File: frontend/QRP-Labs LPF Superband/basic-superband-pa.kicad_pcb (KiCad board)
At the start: 2 copper layers, 64.5 x 60 mm, 82 parts, among them CN1 EDGE, K1 D3002, K2 D3002, P1 BNC, P2 VFWD, P3 Ext PTT, P4 12-13.8v, Q1 FDV301, Q2 FDV301, Q3 RD16HHF1, T2 8:1, T3 4:1, T4 OUT_TRANSF, U1 LP2951-50D

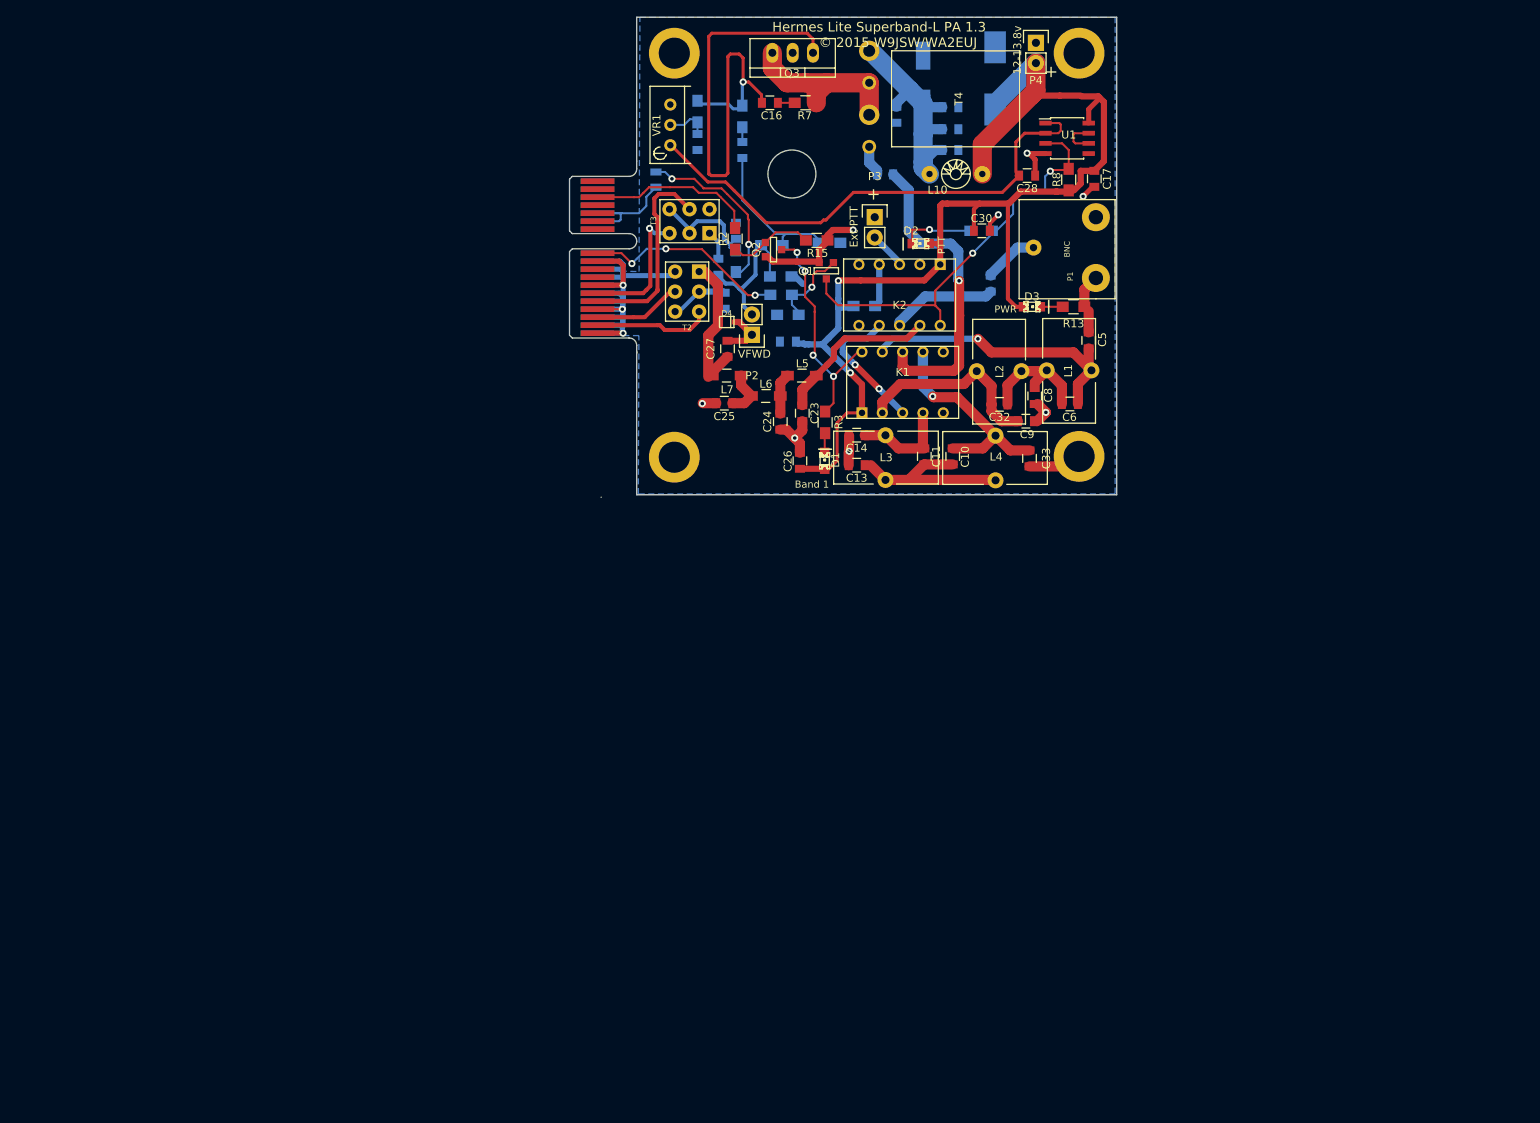
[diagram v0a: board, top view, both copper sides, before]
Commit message: Further updates to the pre-V2 amp
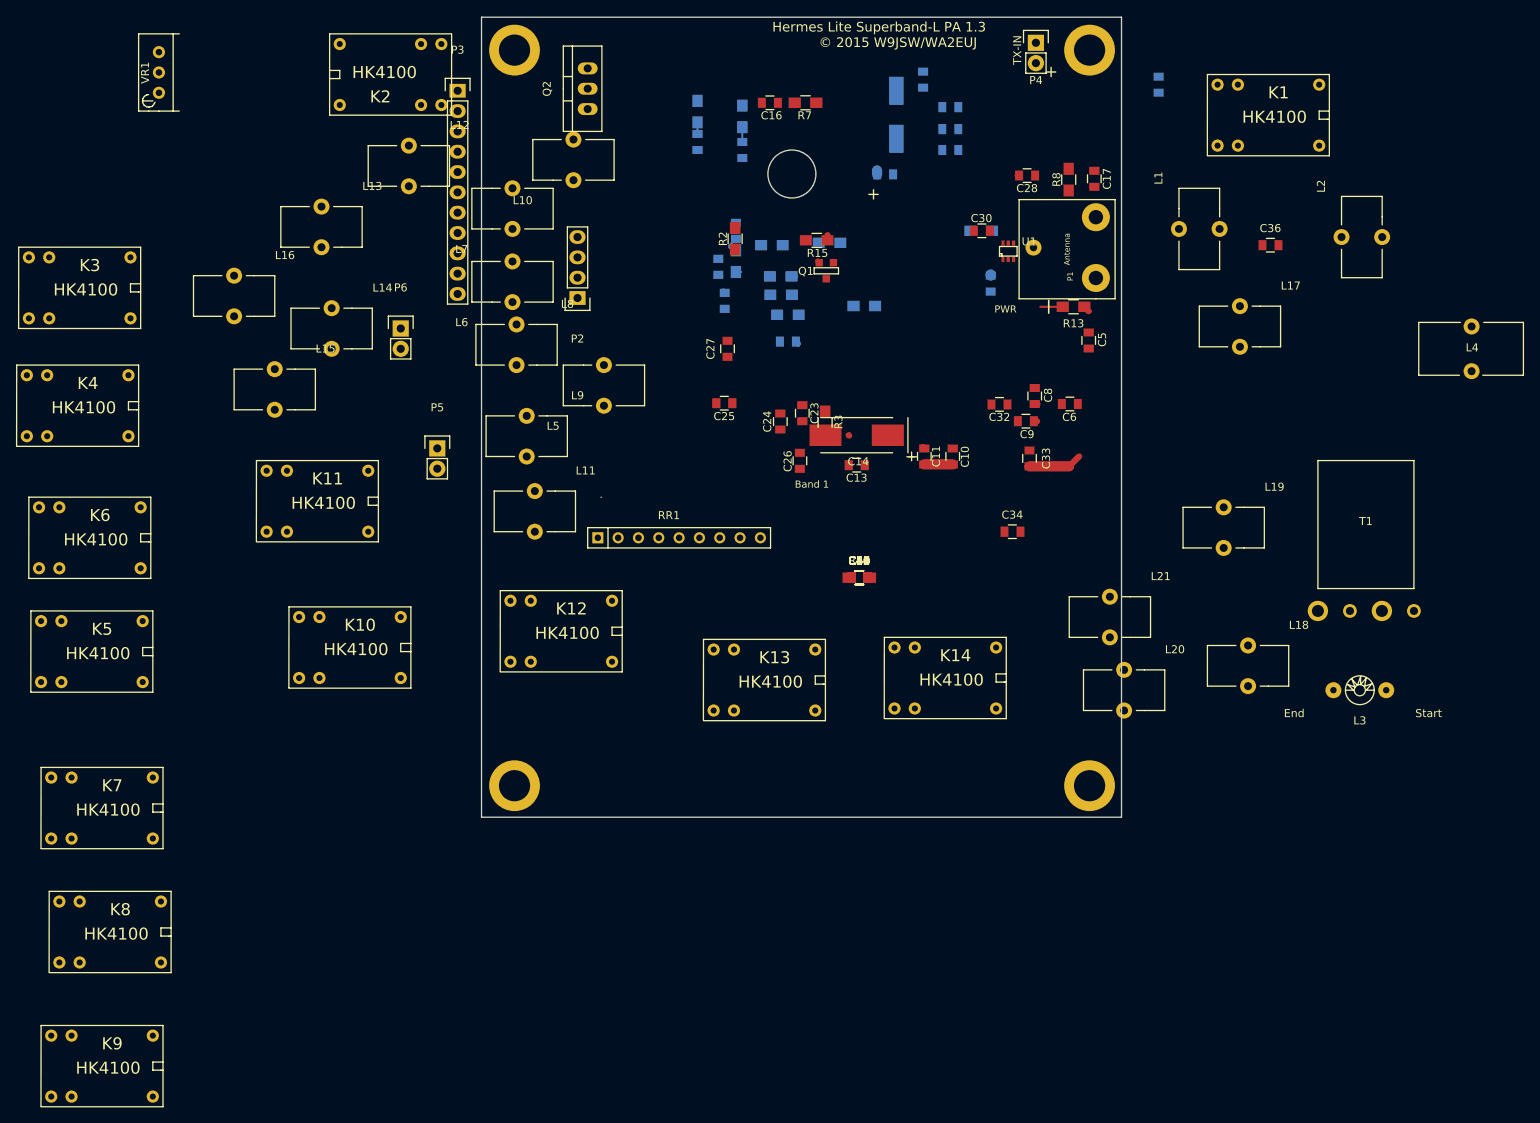
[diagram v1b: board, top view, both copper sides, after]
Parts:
- removed CN1: EDGE, HERMESLITE:EDGE
- removed D1: YEL LED (Band1), LEDs:LED-0805
- removed D2: RED LED (PTT), LEDs:LED-0805
- removed D3: GRN LED (PWR ON), LEDs:LED-0805
- removed D4: DIODESCH2, HERMESLITE:SOD323
- removed FB1: FB, SMD_Packages:SMD-0805
- removed Q3: RD16HHF1, Transistors_TO-220:TO-220_Neutral123_Vertical
- removed T2: 8:1, HERMESLITE:TRANSF
- removed T3: 4:1, HERMESLITE:TRANSF
- removed T4: OUT_TRANSF, HERMESLITE:OUT_TRANSF
- added C34: C, HERMESLITE:C_0805, F.Cu at (181.4, 99.3)
- added C35, C37, C38, C45, C46, C47, C48, C49, C50, C57, C58, C59, C60, C61, C62: C, HERMESLITE:C_0805, F.Cu at (162.2, 105.1)
- added C36: C, HERMESLITE:C_0805, F.Cu at (213.6, 63.5)
- added C39, C40, C41, C42, C43, C44, C51, C52, C53, C54, C55, C56: DNI, HERMESLITE:C_0805, F.Cu at (162.2, 105.1)
- added K10: HK4100, HERMESLITE:HK4100, F.Cu at (98.6, 113.8)
- added K11: HK4100, HERMESLITE:HK4100, F.Cu at (94.5, 95.5)
- added K12: HK4100, HERMESLITE:HK4100, F.Cu at (125.0, 111.8)
- added K13: HK4100, HERMESLITE:HK4100, F.Cu at (150.4, 117.9)
- added K14: HK4100, HERMESLITE:HK4100, F.Cu at (173.0, 117.6)
- added K3: HK4100, HERMESLITE:HK4100, F.Cu at (64.8, 68.8)
- added K4: HK4100, HERMESLITE:HK4100, F.Cu at (64.5, 83.6)
- added K5: HK4100, HERMESLITE:HK4100, F.Cu at (66.3, 114.3)
- added K6: HK4100, HERMESLITE:HK4100, F.Cu at (66.0, 100.1)
- added K7: HK4100, HERMESLITE:HK4100, F.Cu at (67.6, 133.9)
- added K8: HK4100, HERMESLITE:HK4100, F.Cu at (68.6, 149.4)
- added K9: HK4100, HERMESLITE:HK4100, F.Cu at (67.6, 166.1)
- added L11: INDUCTOR, Choke_Toroid_ThroughHole:Choke_Toroid_5x10mm_Vertical, F.Cu at (116.6, 99.3)
- added L12: INDUCTOR, Choke_Toroid_ThroughHole:Choke_Toroid_5x10mm_Vertical, F.Cu at (100.8, 56.1)
- added L13: INDUCTOR, Choke_Toroid_ThroughHole:Choke_Toroid_5x10mm_Vertical, F.Cu at (89.9, 63.8)
- added L14: INDUCTOR, Choke_Toroid_ThroughHole:Choke_Toroid_5x10mm_Vertical, F.Cu at (91.2, 76.5)
- added L15: INDUCTOR, Choke_Toroid_ThroughHole:Choke_Toroid_5x10mm_Vertical, F.Cu at (84.1, 84.1)
- added L16: INDUCTOR, Choke_Toroid_ThroughHole:Choke_Toroid_5x10mm_Vertical, F.Cu at (79.0, 72.4)
- added L17: INDUCTOR, Choke_Toroid_ThroughHole:Choke_Toroid_5x10mm_Vertical, F.Cu at (204.7, 76.2)
- added L18: INDUCTOR, Choke_Toroid_ThroughHole:Choke_Toroid_5x10mm_Vertical, F.Cu at (205.7, 118.6)
- added L19: INDUCTOR, Choke_Toroid_ThroughHole:Choke_Toroid_5x10mm_Vertical, F.Cu at (202.7, 101.3)
- added L20: INDUCTOR, Choke_Toroid_ThroughHole:Choke_Toroid_5x10mm_Vertical, F.Cu at (190.2, 121.7)
- added L21: INDUCTOR, Choke_Toroid_ThroughHole:Choke_Toroid_5x10mm_Vertical, F.Cu at (188.5, 112.5)
- added L8: INDUCTOR, Choke_Toroid_ThroughHole:Choke_Toroid_5x10mm_Vertical, F.Cu at (114.3, 78.5)
- added L9: INDUCTOR, Choke_Toroid_ThroughHole:Choke_Toroid_5x10mm_Vertical, F.Cu at (115.6, 89.9)
- added P5: RX IN, Pin_Headers:Pin_Header_Straight_1x02, F.Cu at (109.5, 88.9)
- added P6: 12-13.8v, Pin_Headers:Pin_Header_Straight_1x02, F.Cu at (104.9, 73.9)
- added R17: 270, Resistors_SMD:R_0805_HandSoldering, F.Cu at (162.2, 105.1)
- added RR1: 10K, Discret:r_pack8, F.Cu at (139.7, 100.1)
- added T1: OUT_TRANSF, HERMESLITE:OUT_TRANSF, F.Cu at (225.6, 109.2)
- C10: value C -> 1uF
- C11, C13, C8, C9: value C -> 0.1uF
- C14: value C -> 47uF 25V; footprint HERMESLITE:C_0805 -> Capacitors_Tantalum_SMD:TantalC_SizeD_EIA-7343_HandSoldering
- C17: value 1uF -> 0.1uF
- C19: value 0.1uF -> 4700pF
- C2: value 0.1 uF -> 78pf
- C20: value 0.1uF -> 10uF 25V; footprint HERMESLITE:C_0805 -> Capacitors_Tantalum_SMD:TantalC_SizeC_EIA-6032_HandSoldering
- C21: value 4700pF -> C
- C22: value 10uF 25V -> C; footprint Capacitors_Tantalum_SMD:TantalC_SizeC_EIA-6032_HandSoldering -> HERMESLITE:C_0805
- C23: value 56pf -> C
- C24, C25: value 156pf -> C
- C26: value 0.1uF -> C
- C27: value 56pf -> DNI
- C28: value 1uF -> DNI
- C29, C30, C31: value 0.1uF -> DNI
- C3: value 0.1 uF -> 12pf
- C32: value C -> DNI
- C4: value 0.1uF -> 150pf
- C5: value C -> 30pf
- C6: value C -> 56pf
- C7: value 47uF 25V -> 1uF; footprint Capacitors_Tantalum_SMD:TantalC_SizeD_EIA-7343_HandSoldering -> HERMESLITE:C_0805
- K1, K2: value D3002 -> HK4100; footprint HERMESLITE:D3002 -> HERMESLITE:HK4100
- L1: value INDUCTOR -> 302.5nH; footprint Choke_Toroid_ThroughHole:Choke_Toroid_6,5x13mm_Vertical -> Choke_Toroid_ThroughHole:Choke_Toroid_5x10mm_Vertical
- L10: value FT37-43 11T #26 -> INDUCTOR; footprint Choke_Toroid_ThroughHole:Choke_Toroid_horizontal_Diameter3-5mm_Amidon-T12 -> Choke_Toroid_ThroughHole:Choke_Toroid_5x10mm_Vertical
- L2: value INDUCTOR -> 250nH; footprint Choke_Toroid_ThroughHole:Choke_Toroid_6,5x13mm_Vertical -> Choke_Toroid_ThroughHole:Choke_Toroid_5x10mm_Vertical
- L3: value INDUCTOR -> FT37-43 11T #26; footprint Choke_Toroid_ThroughHole:Choke_Toroid_6,5x13mm_Vertical -> Choke_Toroid_ThroughHole:Choke_Toroid_horizontal_Diameter3-5mm_Amidon-T12
- L5, L6, L7: footprint Choke_SMD:Choke_SMD_1206_Standard -> Choke_Toroid_ThroughHole:Choke_Toroid_5x10mm_Vertical
- P1: value BNC -> Antenna
- P2: value VFWD -> CONN_01X04; footprint Pin_Headers:Pin_Header_Straight_1x02 -> Pin_Headers:Pin_Header_Straight_1x04
- P3: value Ext PTT -> PA Control; footprint Pin_Headers:Pin_Header_Straight_1x02 -> Pin_Headers:Pin_Header_Straight_1x11
- P4: value 12-13.8v -> TX-IN
- Q2: value FDV301 -> RD16HHF1; footprint HERMESLITE:SOT-23-GDS -> Transistors_TO-220:TO-220_Neutral123_Vertical
- R1: value 499 -> 2.7k
- R10: value 270 -> 18
- R11: value 18 -> 61
- R13, R9: value 4.99k -> 247
- R14: value 4.99k -> 10k
- R15: value 10k -> 6.8
- R2: value 499 -> 120
- R3: value 4.99k -> 51
- R4: value 0 -> 120
- R5: value 6.8 -> 247
- R6: value 10k -> 61
- R7: value 270 -> 247
- R8: value 10k -> 270
- U1: value LP2951-50D -> PE4259-53; footprint Housings_SOIC:SOIC-8_3.9x4.9mm_Pitch1.27mm -> HERMESLITE:sc70-6
- moved K2 69.3 mm to (103.6, 42.2)
- moved VR1 64.3 mm to (74.7, 44.5)
- moved L3 61.8 mm to (224.8, 119.1)
- moved L4 61.1 mm to (232.2, 79.8)
- moved K1 56.6 mm to (213.4, 47.2)
- moved P3 54.5 mm to (112.0, 44.2)
- moved L2 48.2 mm to (227.6, 67.6)
- moved MH 45.7 mm to (119.1, 131.1)
- moved L10 42.9 mm to (131.6, 50.3)
- moved MH 41.2 mm to (191.0, 131.1)
- moved L7 31.9 mm to (124.0, 56.4)
- moved L6 31.5 mm to (124.0, 65.5)
- moved Q2 30.7 mm to (128.3, 43.9)
- moved L1 24.7 mm to (207.3, 66.5)
- moved P2 22.3 mm to (127.0, 70.1)
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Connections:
- C1 pad 1: GND -> Net-(C1-Pad1)
- C10 pad 1: Net-(C10-Pad1) -> GND
- C11 pad 2: Net-(C10-Pad1) -> Net-(C11-Pad2)
- C12 pad 1: GND -> Net-(C12-Pad1)
- C12 pad 2: Net-(C12-Pad2) -> GND
- C13 pad 1: Net-(C10-Pad1) -> Net-(C12-Pad1)
- C14 pad 1: Net-(C11-Pad1) -> Net-(C12-Pad1)
- C15 pad 2: Net-(C15-Pad2) -> TX-OUT
- C16 pad 1: Net-(C16-Pad1) -> GND
- C17 pad 1: Net-(C17-Pad1) -> GND
- C17 pad 2: GND -> Net-(C16-Pad2)
- C18 pad 1: Net-(C18-Pad1) -> GND
- C18 pad 2: Net-(C18-Pad2) -> Net-(C16-Pad2)
- C19 pad 2: Net-(C1-Pad2) -> Net-(C16-Pad2)
- C2 pad 1: Net-(C2-Pad1) -> Net-(C1-Pad2)
- C20 pad 1: GND -> Net-(C16-Pad2)
- C20 pad 2: Net-(C1-Pad2) -> GND
- C21 pad 1: GND -> Net-(C21-Pad1)
- C21 pad 2: Net-(C1-Pad2) -> GND
- C22 pad 1: Net-(C1-Pad2) -> Net-(C22-Pad1)
- C26 pad 1: GND -> Net-(C26-Pad1)
- C26 pad 2: Net-(C17-Pad1) -> GND
- C27 pad 2: GND -> Net-(C21-Pad1)
- C28 pad 1: GND -> Net-(C28-Pad1)
- C28 pad 2: Net-(C28-Pad2) -> Net-(C22-Pad1)
- C29 pad 2: Net-(C29-Pad2) -> Net-(C23-Pad1)
- C3 pad 2: GND -> Net-(C1-Pad2)
- C30 pad 1: Net-(C17-Pad1) -> Net-(C30-Pad1)
- C30 pad 2: GND -> Net-(C24-Pad1)
- C31 pad 1: Net-(C17-Pad1) -> Net-(C31-Pad1)
- C31 pad 2: GND -> Net-(C25-Pad1)
- C32 pad 2: Net-(C32-Pad2) -> Net-(C26-Pad1)
- C33 pad 1: Net-(C10-Pad2) -> Net-(C27-Pad1)
- C4 pad 1: Net-(C4-Pad1) -> Net-(C3-Pad1)
- C4 pad 2: Net-(C4-Pad2) -> GND
- C5 pad 2: GND -> Net-(C3-Pad1)
- C6 pad 2: Net-(C32-Pad1) -> GND
- C7 pad 1: Net-(C17-Pad1) -> GND
- C7 pad 2: GND -> +5V
- C8 pad 1: Net-(C32-Pad1) -> Net-(C8-Pad1)
- C8 pad 2: GND -> Net-(C8-Pad2)
- C9 pad 1: Net-(C32-Pad2) -> GND
- C9 pad 2: GND -> Net-(C9-Pad2)
- K1 pad 1: Net-(C17-Pad1) -> Net-(K1-Pad1)
- K1 pad 2: Net-(C32-Pad2) -> /PTT
- K1 pad 3: Net-(K1-Pad3) -> Net-(C5-Pad1)
- K1 pad 4: Net-(C11-Pad1) -> Net-(K1-Pad4)
- K1 pad 5: (no net) -> +5V
- K1 pad 6: (no net) -> TX-IN
- K2 pad 1: Net-(C17-Pad1) -> GND
- K2 pad 2: GND -> /Band0
- K2 pad 4: Net-(K2-Pad4) -> Net-(C21-Pad1)
- K2 pad 5: (no net) -> +5V
- K2 pad 6: (no net) -> TX-OUT
- L1 pad 1: Net-(C5-Pad1) -> Net-(C1-Pad2)
- L1 pad 2: Net-(C32-Pad1) -> Net-(C3-Pad1)
- L10 pad 1: Net-(C17-Pad1) -> Net-(C27-Pad1)
- L10 pad 2: Net-(C1-Pad2) -> Net-(C39-Pad1)
- L2 pad 1: Net-(C32-Pad1) -> Net-(C3-Pad1)
- L2 pad 2: Net-(C32-Pad2) -> Net-(C5-Pad1)
- L3 pad 1: Net-(C11-Pad1) -> Net-(C12-Pad1)
- L3 pad 2: Net-(C10-Pad1) -> Net-(C16-Pad2)
- L4 pad 1: Net-(C10-Pad1) -> Net-(C21-Pad1)
- L4 pad 2: Net-(C10-Pad2) -> Net-(C27-Pad1)
- L5 pad 1: Net-(C23-Pad1) -> Net-(C22-Pad1)
- L5 pad 2: Net-(C24-Pad1) -> Net-(C28-Pad1)
- L6 pad 1: Net-(C24-Pad1) -> Net-(C23-Pad1)
- L6 pad 2: Net-(C25-Pad1) -> Net-(C29-Pad1)
- L7 pad 1: Net-(C25-Pad1) -> Net-(C24-Pad1)
- L7 pad 2: Net-(C27-Pad1) -> Net-(C30-Pad1)
- P1 pad 1: Net-(C18-Pad1) -> Net-(C1-Pad1)
- P2 pad 2: Net-(C4-Pad1) -> +3.3V
- P3 pad 1: GND -> /Band0
- P3 pad 2: Net-(K2-Pad3) -> /Band1
- P4 pad 2: Net-(C17-Pad1) -> Net-(P4-Pad2)
- Q1 pad D: /PTT -> +5V
- Q1 pad G: Net-(Q1-PadG) -> /PTT
- Q1 pad S: GND -> Net-(C10-Pad2)
- R1 pad 1: Net-(Q1-PadG) -> Net-(R1-Pad1)
- R1 pad 2: PTT -> Net-(C1-Pad2)
- R10 pad 1: GND -> Net-(C8-Pad2)
- R10 pad 2: Net-(C4-Pad1) -> Net-(P4-Pad2)
- R11 pad 1: Net-(C15-Pad2) -> Net-(R11-Pad1)
- R11 pad 2: Net-(C4-Pad1) -> Net-(R11-Pad2)
- R12 pad 2: Net-(C15-Pad2) -> Net-(C8-Pad2)
- R13 pad 2: Net-(D3-Pad2) -> Net-(R11-Pad1)
- R14 pad 1: Net-(K2-Pad4) -> /PTT
- R14 pad 2: Net-(C17-Pad1) -> +5V
- R15 pad 1: GND -> Net-(C11-Pad2)
- R15 pad 2: Net-(Q2-PadG) -> Net-(C8-Pad1)
- R16 pad 1: GND -> Net-(C11-Pad2)
- R16 pad 2: Net-(Q1-PadG) -> Net-(C9-Pad2)
- R2 pad 1: Net-(Q2-PadG) -> GND
- R2 pad 2: USEROUT4 -> Net-(R1-Pad1)
- R3 pad 1: BAND1 -> Net-(R3-Pad1)
- R3 pad 2: Net-(D1-Pad2) -> Net-(R1-Pad1)
- R4 pad 1: Net-(C3-Pad1) -> GND
- R4 pad 2: Net-(FB1-Pad2) -> Net-(R3-Pad1)
- R5 pad 1: Net-(C16-Pad2) -> GND
- R5 pad 2: Net-(C15-Pad1) -> Net-(R3-Pad1)
- R6 pad 1: Net-(C16-Pad2) -> Net-(R11-Pad2)
- R6 pad 2: Net-(C12-Pad2) -> Net-(R3-Pad1)
- R7 pad 1: Net-(Q3-Pad3) -> GND
- R7 pad 2: Net-(C16-Pad1) -> Net-(R11-Pad2)
- R8 pad 1: /PTT -> GND
- R8 pad 2: Net-(C17-Pad1) -> Net-(P4-Pad2)
- R9 pad 1: /PTT -> GND
- R9 pad 2: Net-(D2-Pad2) -> Net-(R11-Pad2)
- U1 pad 1: Net-(C28-Pad2) -> Net-(R11-Pad1)
- U1 pad 2: Net-(C28-Pad2) -> GND
- U1 pad 3: /PTT -> Net-(U1-Pad3)
- U1 pad 4: GND -> CTRL
- U1 pad 5: Net-(U1-Pad5) -> Net-(K1-Pad1)
- U1 pad 6: Net-(U1-Pad6) -> +3.3V
- VR1 pad 1: Net-(C28-Pad2) -> Net-(C10-Pad2)
- VR1 pad 2: Net-(C12-Pad2) -> Net-(C9-Pad2)
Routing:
- net Net-(C17-Pad1): track 147.8 -> 0.00 mm, vias 2 -> 0
- net GND: track 128.6 -> 11.4 mm, vias 11 -> 0
- net Net-(C16-Pad2): track 67.7 -> 0.27 mm, vias 1 -> 0
- net Net-(C28-Pad2): track 63.8 -> 0.00 mm
- net /PTT: track 52.3 -> 0.00 mm, vias 2 -> 0
- net Net-(C29-Pad1): track 39.0 -> 0.00 mm, vias 1 -> 0
- net Net-(C5-Pad1): track 36.6 -> 0.00 mm, vias 1 -> 0
- net Net-(C1-Pad2): track 30.7 -> 0.21 mm
- net BAND1: track 29.3 -> 0.00 mm, vias 4 -> 0
- net Net-(C10-Pad2): track 29.2 -> 0.19 mm, vias 1 -> 0
- net Net-(C10-Pad1): track 26.3 -> 0.00 mm
- net PTT: track 25.3 -> 0.00 mm, vias 3 -> 0
- net Net-(CN1-PadB5): track 25.3 -> 0.00 mm
- net Net-(C32-Pad2): track 24.3 -> 0.00 mm
- net Net-(FB1-Pad2): track 22.0 -> 0.00 mm, vias 2 -> 0
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- removed copper zone on B.Cu, net GND
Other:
- board size 64.5 x 60 mm -> 80 x 100 mm
- board text removed: "PTT"
